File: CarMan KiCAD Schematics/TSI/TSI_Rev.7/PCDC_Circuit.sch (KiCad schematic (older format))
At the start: 59 parts, among them IC1 TS431ILT, K1 APAN3105, Q1 ZVP1320F, Q3 SI1302DL-T1-E3, U10 MC7805BDTRKG, U12 REF3033, U19 SN74HC00APWR, U21 TLV2464CDR, U27 TLP293, U34 TLP293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

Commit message: TSI REV7 Final Schematic before Layout
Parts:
- removed TP19: PC_Control, TestPoint:TestPoint_Pad_D3.0mm, symbol TSI_Rev.5-rescue:TestPoint-Connector
- removed TP4: TSV_Ready, TestPoint:TestPoint_Pad_D3.0mm, symbol TSI_Rev.5-rescue:TestPoint-Connector
- removed TP5: MC_95%, TestPoint:TestPoint_Pad_D3.0mm, symbol TSI_Rev.5-rescue:TestPoint-Connector
- removed TP6: SLOOP_HV, TestPoint:TestPoint_Pad_D3.0mm, symbol TSI_Rev.5-rescue:TestPoint-Connector
- added J25: PC Test Points, Connector_PinSocket_2.54mm:PinSocket_1x05_P2.54mm_Vertical, symbol Connector_Generic:Conn_01x05
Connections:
- net DC_RELAY-: now also J25.1 (Pin_1)
- net MC_95%: now also J25.3 (Pin_3)
- net PC_Control: now also J25.5 (Pin_5)
- net Safety_Loop_HV: now also J25.4 (Pin_4)
- net TSV_Ready: now also J25.2 (Pin_2)
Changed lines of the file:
@@
 TSV Minimum Voltage Check
 Connection ~ 7475 6800
-Wire Wire Line
-	7025 6275 7025 6375
-Wire Wire Line
-	7025 6375 7825 6375
-$Comp
-L TSI_Rev.5-rescue:TestPoint-Connector TP?
-U 1 1 63DE42FD
-P 7025 6275
-AR Path="/5FC85F57/63DE42FD" Ref="TP?"  Part="1"
-AR Path="/6196BF15/63DE42FD" Ref="TP4"  Part="1"
-F 0 "TP4" H 6950 6475 50  0000 L CNN
-F 1 "TSV_Ready" H 6675 6400 50  0001 L CNN
-F 2 "TestPoint:TestPoint_Pad_D3.0mm" H 7225 6275 50  0001 C CNN
-F 3 "~" H 7225 6275 50  0001 C CNN
-	1    7025 6275
-	1    0    0    -1
-$EndComp
-$Comp
-L TSI_Rev.5-rescue:TestPoint-Connector TP?
-U 1 1 63E1488B
-P 7250 6275
-AR Path="/5FC85F57/63E1488B" Ref="TP?"  Part="1"
-AR Path="/6196BF15/63E1488B" Ref="TP5"  Part="1"
-F 0 "TP5" H 7175 6475 50  0000 L CNN
-F 1 "MC_95%" H 7300 6375 50  0001 L CNN
-F 2 "TestPoint:TestPoint_Pad_D3.0mm" H 7450 6275 50  0001 C CNN
-F 3 "~" H 7450 6275 50  0001 C CNN
-	1    7250 6275
-	1    0    0    -1
-$EndComp
-Wire Wire Line
-	7250 6275 7250 6575
-Wire Wire Line
-	7250 6575 7825 6575
 $Comp
 L TSI_Rev.5-rescue:74HC00-74xx U19
@@
 	21625 1850 21625 2300
 Connection ~ 21625 1850
-$Comp
-L TSI_Rev.5-rescue:TestPoint-Connector TP?
-U 1 1 6464F7D3
-P 7475 6275
-AR Path="/5FC85F57/6464F7D3" Ref="TP?"  Part="1"
-AR Path="/6196BF15/6464F7D3" Ref="TP6"  Part="1"
-F 0 "TP6" H 7425 6475 50  0000 L CNN
-F 1 "SLOOP_HV" V 7550 6225 50  0001 L CNN
-F 2 "TestPoint:TestPoint_Pad_D3.0mm" H 7675 6275 50  0001 C CNN
-F 3 "~" H 7675 6275 50  0001 C CNN
-	1    7475 6275
-	1    0    0    -1
-$EndComp
-Wire Wire Line
-	7475 6800 7475 6275
 Wire Wire Line
 	6000 12900 6250 12900
@@
 Text Notes 4525 6250 0    59   ~ 0
 MC Voltage 95% Check
-Connection ~ 7025 6375
-Connection ~ 7250 6575
 Text Notes 7575 5475 0    197  ~ 0
 PRE-CHARGE LOGIC CIRCUIT
@@
 Text Label 13250 7150 2    59   ~ 0
 PC_Control
-$Comp
-L TSI_Rev.5-rescue:TestPoint-Connector TP?
-U 1 1 60D4CBAD
-P 12725 7000
-AR Path="/5FC85F57/60D4CBAD" Ref="TP?"  Part="1"
-AR Path="/6196BF15/60D4CBAD" Ref="TP19"  Part="1"
-F 0 "TP19" H 12675 7200 50  0000 L CNN
-F 1 "PC_Control" H 12750 7050 50  0001 L CNN
-F 2 "TestPoint:TestPoint_Pad_D3.0mm" H 12925 7000 50  0001 C CNN
-F 3 "~" H 12925 7000 50  0001 C CNN
-	1    12725 7000
-	1    0    0    -1
-$EndComp
-Wire Wire Line
-	12725 7000 12725 7150
 Wire Bus Line
 	13700 5475 13700 5675
@@
 Text Label 8720 12025 2    50   ~ 0
 IO_Ground
-Connection ~ 12725 7150
 Wire Wire Line
 	15100 6150 15450 6150
@@
 Wire Wire Line
 	15450 6150 15850 6150
-Wire Wire Line
-	12725 7150 14400 7150
 Wire Wire Line
 	14400 8900 13900 8900
@@
 Connection ~ 6350 7775
 Connection ~ 6100 6375
-Wire Wire Line
-	6100 6375 7025 6375
 Connection ~ 6350 6575
-Wire Wire Line
-	6350 6575 7250 6575
 Wire Wire Line
 	5450 6575 6350 6575
@@
 Connection ~ 6625 6800
 Wire Wire Line
-	6625 6800 7475 6800
+	6625 6800 7300 6800
 Wire Wire Line
 	6350 7775 6625 7775
@@
 	5875 5075 14025 5075
 Connection ~ 14400 7150
-Wire Wire Line
-	11750 7150 12725 7150
 Connection ~ 11750 7150
 Text Notes 16100 5775 2    31   ~ 0
@@
 Wire Notes Line
 	18075 3600 22100 3600
+$Comp
+L Connector_Generic:Conn_01x05 J25
+U 1 1 62432C90
+P 7100 5600
+F 0 "J25" V 7275 5725 50  0000 R CNN
+F 1 "PC Test Points" V 7200 5725 50  0000 R CNN
+F 2 "Connector_PinSocket_2.54mm:PinSocket_1x05_P2.54mm_Vertical" H 7100 5600 50  0001 C CNN
+F 3 "~" H 7100 5600 50  0001 C CNN
+	1    7100 5600
+	0    -1   -1   0
+$EndComp
+Wire Wire Line
+	6100 6375 7000 6375
+Wire Wire Line
+	6350 6575 7100 6575
+Wire Wire Line
+	7000 5800 7000 6375
+Connection ~ 7000 6375
+Wire Wire Line
+	7000 6375 7825 6375
+Wire Wire Line
+	7100 5800 7100 6575
+Connection ~ 7100 6575
+Wire Wire Line
+	7100 6575 7825 6575
+Wire Wire Line
+	7200 5800 7200 6275
+Wire Wire Line
+	7200 6275 7300 6275
+Wire Wire Line
+	7300 6275 7300 6800
+Connection ~ 7300 6800
+Wire Wire Line
+	7300 6800 7475 6800
+Wire Wire Line
+	7300 5800 7800 5800
+Wire Wire Line
+	6900 5800 6900 5900
+Wire Wire Line
+	6900 5900 6425 5900
+Text Label 7800 5800 2    39   ~ 0
+PC_Control
+Text Label 6425 5900 0    39   ~ 0
+IO_Ground
+Wire Wire Line
+	11750 7150 14400 7150
 $EndSCHEMATC

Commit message: Fixed annotation issue
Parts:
- renumbered J25 to J29
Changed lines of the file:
@@
 	18075 3600 22100 3600
 $Comp
-L Connector_Generic:Conn_01x05 J25
+L Connector_Generic:Conn_01x05 J29
 U 1 1 62432C90
 P 7100 5600
-F 0 "J25" V 7275 5725 50  0000 R CNN
+F 0 "J29" V 7275 5725 50  0000 R CNN
 F 1 "PC Test Points" V 7200 5725 50  0000 R CNN
 F 2 "Connector_PinSocket_2.54mm:PinSocket_1x05_P2.54mm_Vertical" H 7100 5600 50  0001 C CNN

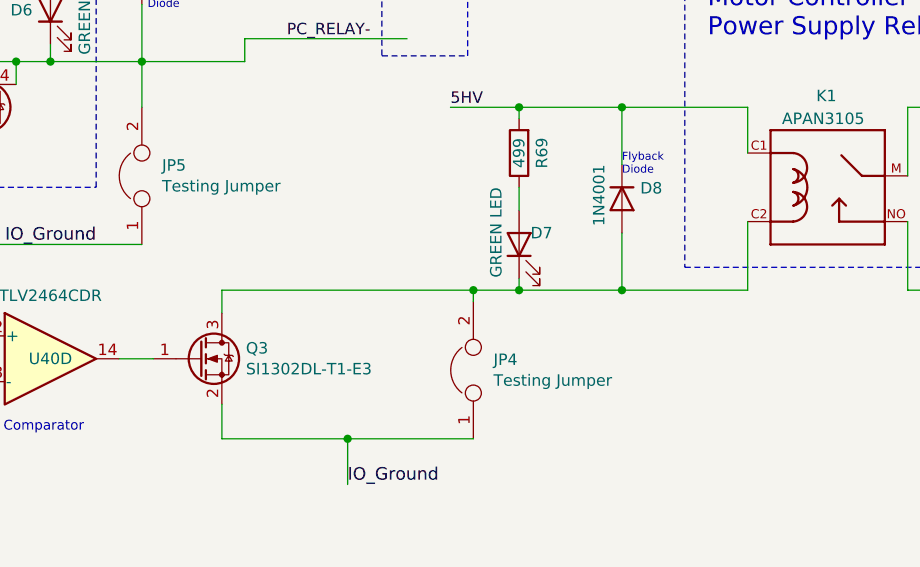
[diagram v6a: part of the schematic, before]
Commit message: Updated Schematic and removed extra footprints from PCB. Ready to begin routing new elements in.
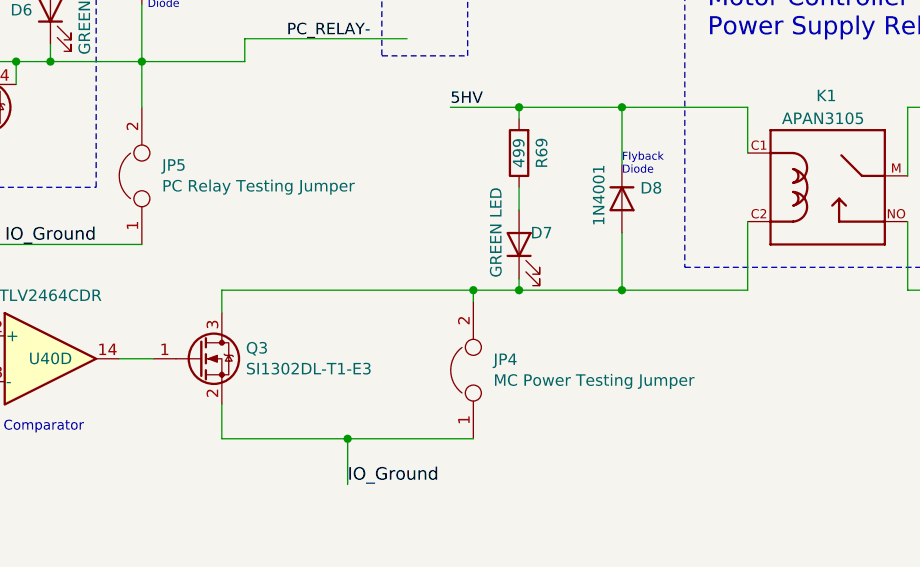
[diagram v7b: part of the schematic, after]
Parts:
- J29: footprint Connector_PinSocket_2.54mm:PinSocket_1x05_P2.54mm_Vertical -> Connector_PinHeader_2.54mm:PinHeader_1x05_P2.54mm_Vertical
- JP4: value Testing Jumper -> MC Power Testing Jumper
- JP5: value Testing Jumper -> PC Relay Testing Jumper
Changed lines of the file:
@@
 P 17300 8300
 F 0 "JP4" V 17346 8212 50  0000 R CNN
-F 1 "Testing Jumper" V 17255 8212 50  0000 R CNN
+F 1 "MC Power Testing Jumper" V 17255 8212 50  0000 R CNN
 F 2 "Connector_PinHeader_2.54mm:PinHeader_1x02_P2.54mm_Vertical" H 17300 8300 50  0001 C CNN
 F 3 "~" H 17300 8300 50  0001 C CNN
@@
 P 15850 7450
 F 0 "JP5" V 15896 7362 50  0000 R CNN
-F 1 "Testing Jumper" V 15805 7362 50  0000 R CNN
+F 1 "PC Relay Testing Jumper" V 15805 7362 50  0000 R CNN
 F 2 "Connector_PinHeader_2.54mm:PinHeader_1x02_P2.54mm_Vertical" H 15850 7450 50  0001 C CNN
 F 3 "~" H 15850 7450 50  0001 C CNN
@@
 F 0 "J29" V 7275 5725 50  0000 R CNN
 F 1 "PC Test Points" V 7200 5725 50  0000 R CNN
-F 2 "Connector_PinSocket_2.54mm:PinSocket_1x05_P2.54mm_Vertical" H 7100 5600 50  0001 C CNN
+F 2 "Connector_PinHeader_2.54mm:PinHeader_1x05_P2.54mm_Vertical" H 7100 5600 50  0001 C CNN
 F 3 "~" H 7100 5600 50  0001 C CNN
 	1    7100 5600
